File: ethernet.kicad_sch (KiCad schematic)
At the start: 37 parts, among them J200 RJ45_Hanrun_HR911105A_Horizon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, U200 LAN8742A, U201 USBLC6-4SC6, Y200 25MHz

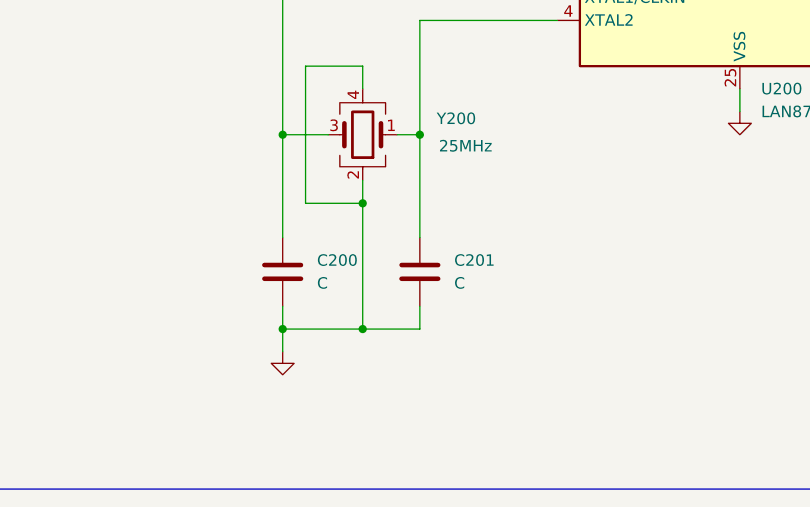
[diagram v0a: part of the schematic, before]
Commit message: Footprints added
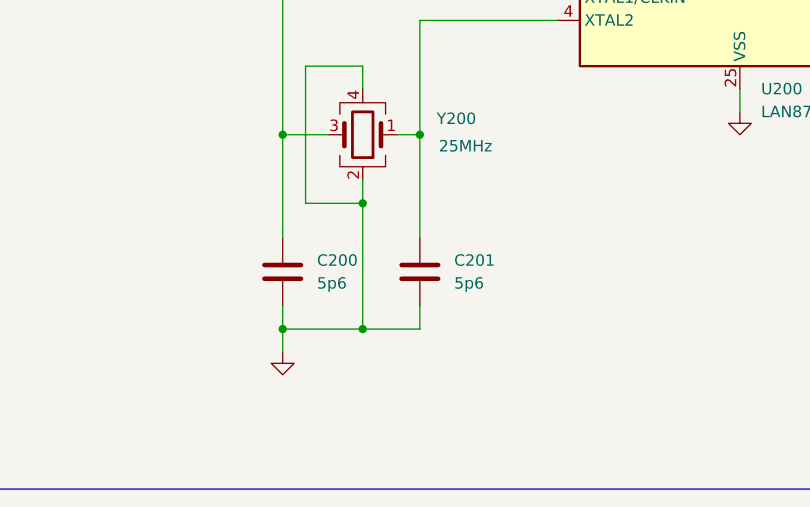
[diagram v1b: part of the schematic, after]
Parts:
- C200, C201: value C -> 5p6; footprint (none) -> Capacitor_SMD:C_01005_0402Metric
- C202: footprint (none) -> Capacitor_SMD:C_0201_0603Metric
- C203, C204, C205, C206, C207, C208, C209, C210, C211, C212: footprint (none) -> Capacitor_SMD:C_01005_0402Metric
- JP200: footprint (none) -> Jumper:SolderJumper-2_P1.3mm_Bridged_Pad1.0x1.5mm
- R200, R201, R202, R203, R204, R205, R206, R207, R208, R209, R210, R211, R212, R213, R214, R215, R216, R217, R218: footprint (none) -> Resistor_SMD:R_01005_0402Metric
- Y200: footprint (none) -> Library:CRYSTAL-SMD_4P-L2.0-W1.6-BL
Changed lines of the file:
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@@
 			)
 		)
-		(property "Footprint" ""
+		(property "Footprint" "Resistor_SMD:R_01005_0402Metric"
 			(at 40.894 85.344 90)
 			(effects
@@
 			)
 		)
-		(property "Value" "C"
+		(property "Value" "5p6"
 			(at 74.93 140.9699 0)
 			(effects
@@
 			)
 		)
-		(property "Footprint" ""
+		(property "Footprint" "Capacitor_SMD:C_01005_0402Metric"
 			(at 72.0852 143.51 0)
 			(effects
@@
 			)
 		)
-		(property "Footprint" ""
+		(property "Footprint" "Capacitor_SMD:C_0201_0603Metric"
 			(at 129.2352 50.8 0)
 			(effects
@@
 			)
 		)
-		(property "Footprint" ""
+		(property "Footprint" "Capacitor_SMD:C_01005_0402Metric"
 			(at 187.6552 97.79 0)
 			(effects
@@
 			)
 		)
-		(property "Footprint" ""
+		(property "Footprint" "Resistor_SMD:R_01005_0402Metric"
 			(at 181.356 71.374 90)
 			(effects
@@
 			)
 		)
-		(property "Footprint" ""
+		(property "Footprint" "Resistor_SMD:R_01005_0402Metric"
 			(at 40.894 103.124 90)
 			(effects
@@
 			)
 		)
-		(property "Footprint" ""
+		(property "Footprint" "Capacitor_SMD:C_01005_0402Metric"
 			(at 140.6652 50.8 0)
 			(effects
@@
 			)
 		)
-		(property "Footprint" ""
+		(property "Footprint" "Capacitor_SMD:C_01005_0402Metric"
 			(at 163.5252 50.8 0)
 			(effects
@@
 			)
 		)
-		(property "Footprint" ""
+		(property "Footprint" "Resistor_SMD:R_01005_0402Metric"
 			(at 40.894 87.884 90)
 			(effects
@@
 			)
 		)
-		(property "Footprint" ""
+		(property "Footprint" "Capacitor_SMD:C_01005_0402Metric"
 			(at 174.9552 50.8 0)
 			(effects
@@
 			)
 		)
-		(property "Footprint" ""
+		(property "Footprint" "Resistor_SMD:R_01005_0402Metric"
 			(at 40.894 82.804 90)
 			(effects
@@
 			)
 		)
-		(property "Footprint" ""
+		(property "Footprint" "Capacitor_SMD:C_01005_0402Metric"
 			(at 210.5152 97.79 0)
 			(effects
@@
 			)
 		)
-		(property "Footprint" ""
+		(property "Footprint" "Resistor_SMD:R_01005_0402Metric"
 			(at 215.646 71.374 90)
 			(effects
@@
 			)
 		)
-		(property "Footprint" ""
+		(property "Footprint" "Capacitor_SMD:C_01005_0402Metric"
 			(at 185.1152 152.4 0)
 			(effects
@@
 			)
 		)
-		(property "Footprint" ""
+		(property "Footprint" "Resistor_SMD:R_01005_0402Metric"
 			(at 163.576 100.584 90)
 			(effects
@@
 			)
 		)
-		(property "Footprint" ""
+		(property "Footprint" "Library:CRYSTAL-SMD_4P-L2.0-W1.6-BL"
 			(at 80.01 124.46 0)
 			(effects
@@
 			)
 		)
-		(property "Footprint" ""
+		(property "Footprint" "Resistor_SMD:R_01005_0402Metric"
 			(at 230.886 152.654 90)
 			(effects
@@
 			)
 		)
-		(property "Value" "C"
+		(property "Value" "5p6"
 			(at 90.17 140.9699 0)
 			(effects
@@
 			)
 		)
-		(property "Footprint" ""
+		(property "Footprint" "Capacitor_SMD:C_01005_0402Metric"
 			(at 87.3252 143.51 0)
 			(effects
@@
 			)
 		)
-		(property "Footprint" ""
+		(property "Footprint" "Resistor_SMD:R_01005_0402Metric"
 			(at 185.166 123.444 90)
 			(effects
@@
 			)
 		)
-		(property "Footprint" ""
+		(property "Footprint" "Resistor_SMD:R_01005_0402Metric"
 			(at 192.786 71.374 90)
 			(effects
@@
 			)
 		)
-		(property "Footprint" ""
+		(property "Footprint" "Capacitor_SMD:C_01005_0402Metric"
 			(at 152.0952 50.8 0)
 			(effects
@@
 			)
 		)
-		(property "Footprint" ""
+		(property "Footprint" "Resistor_SMD:R_01005_0402Metric"
 			(at 69.596 70.104 90)
 			(effects
@@
 			)
 		)
-		(property "Footprint" ""
+		(property "Footprint" "Resistor_SMD:R_01005_0402Metric"
 			(at 257.556 138.684 90)
 			(effects
@@
 			)
 		)
-		(property "Footprint" ""
+		(property "Footprint" "Capacitor_SMD:C_01005_0402Metric"
 			(at 254.9652 78.74 0)
 			(effects
@@
 			)
 		)
-		(property "Footprint" ""
+		(property "Footprint" "Capacitor_SMD:C_01005_0402Metric"
 			(at 199.0852 97.79 0)
 			(effects
@@
 			)
 		)
-		(property "Footprint" ""
+		(property "Footprint" "Capacitor_SMD:C_01005_0402Metric"
 			(at 176.2252 97.79 0)
 			(effects
@@
 			)
 		)
-		(property "Footprint" ""
+		(property "Footprint" "Resistor_SMD:R_01005_0402Metric"
 			(at 143.256 108.204 90)
 			(effects
@@
 			)
 		)
-		(property "Footprint" ""
+		(property "Footprint" "Jumper:SolderJumper-2_P1.3mm_Bridged_Pad1.0x1.5mm"
 			(at 40.64 101.6 0)
 			(effects
@@
 			)
 		)
-		(property "Footprint" ""
+		(property "Footprint" "Resistor_SMD:R_01005_0402Metric"
 			(at 78.486 70.104 90)
 			(effects
@@
 			)
 		)
-		(property "Footprint" ""
+		(property "Footprint" "Resistor_SMD:R_01005_0402Metric"
 			(at 248.666 148.844 90)
 			(effects
@@
 			)
 		)
-		(property "Footprint" ""
+		(property "Footprint" "Resistor_SMD:R_01005_0402Metric"
 			(at 51.816 70.104 90)
 			(effects
@@
 			)
 		)
-		(property "Footprint" ""
+		(property "Footprint" "Resistor_SMD:R_01005_0402Metric"
 			(at 204.216 71.374 90)
 			(effects
@@
 			)
 		)
-		(property "Footprint" ""
+		(property "Footprint" "Resistor_SMD:R_01005_0402Metric"
 			(at 60.706 70.104 90)
 			(effects
@@
 			)
 		)
-		(property "Footprint" ""
+		(property "Footprint" "Resistor_SMD:R_01005_0402Metric"
 			(at 87.376 70.104 90)
 			(effects

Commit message: Some changes to power circuitry, more layout
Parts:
- C200, C201, C203, C204, C205, C206, C207, C208, C209, C210, C211, C212: footprint Capacitor_SMD:C_01005_0402Metric -> Capacitor_SMD:C_0402_1005Metric
- C202: footprint Capacitor_SMD:C_0201_0603Metric -> Capacitor_SMD:C_0603_1608Metric
- R200, R201, R202, R203, R204, R205, R206, R207, R208, R209, R210, R211, R212, R213, R214, R215, R216, R217, R218: footprint Resistor_SMD:R_01005_0402Metric -> Resistor_SMD:R_0402_1005Metric
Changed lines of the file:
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@@
 			)
 		)
-		(property "Footprint" "Resistor_SMD:R_01005_0402Metric"
+		(property "Footprint" "Resistor_SMD:R_0402_1005Metric"
 			(at 40.894 85.344 90)
 			(effects
@@
 			)
 		)
-		(property "Footprint" "Capacitor_SMD:C_01005_0402Metric"
+		(property "Footprint" "Capacitor_SMD:C_0402_1005Metric"
 			(at 72.0852 143.51 0)
 			(effects
@@
 			)
 		)
-		(property "Footprint" "Capacitor_SMD:C_0201_0603Metric"
+		(property "Footprint" "Capacitor_SMD:C_0603_1608Metric"
 			(at 129.2352 50.8 0)
 			(effects
@@
 			)
 		)
-		(property "Footprint" "Capacitor_SMD:C_01005_0402Metric"
+		(property "Footprint" "Capacitor_SMD:C_0402_1005Metric"
 			(at 187.6552 97.79 0)
 			(effects
@@
 			)
 		)
-		(property "Footprint" "Resistor_SMD:R_01005_0402Metric"
+		(property "Footprint" "Resistor_SMD:R_0402_1005Metric"
 			(at 181.356 71.374 90)
 			(effects
@@
 			)
 		)
-		(property "Footprint" "Resistor_SMD:R_01005_0402Metric"
+		(property "Footprint" "Resistor_SMD:R_0402_1005Metric"
 			(at 40.894 103.124 90)
 			(effects
@@
 			)
 		)
-		(property "Footprint" "Capacitor_SMD:C_01005_0402Metric"
+		(property "Footprint" "Capacitor_SMD:C_0402_1005Metric"
 			(at 140.6652 50.8 0)
 			(effects
@@
 			)
 		)
-		(property "Footprint" "Capacitor_SMD:C_01005_0402Metric"
+		(property "Footprint" "Capacitor_SMD:C_0402_1005Metric"
 			(at 163.5252 50.8 0)
 			(effects
@@
 			)
 		)
-		(property "Footprint" "Resistor_SMD:R_01005_0402Metric"
+		(property "Footprint" "Resistor_SMD:R_0402_1005Metric"
 			(at 40.894 87.884 90)
 			(effects
@@
 			)
 		)
-		(property "Footprint" "Capacitor_SMD:C_01005_0402Metric"
+		(property "Footprint" "Capacitor_SMD:C_0402_1005Metric"
 			(at 174.9552 50.8 0)
 			(effects
@@
 			)
 		)
-		(property "Footprint" "Resistor_SMD:R_01005_0402Metric"
+		(property "Footprint" "Resistor_SMD:R_0402_1005Metric"
 			(at 40.894 82.804 90)
 			(effects
@@
 			)
 		)
-		(property "Footprint" "Capacitor_SMD:C_01005_0402Metric"
+		(property "Footprint" "Capacitor_SMD:C_0402_1005Metric"
 			(at 210.5152 97.79 0)
 			(effects
@@
 			)
 		)
-		(property "Footprint" "Resistor_SMD:R_01005_0402Metric"
+		(property "Footprint" "Resistor_SMD:R_0402_1005Metric"
 			(at 215.646 71.374 90)
 			(effects
@@
 			)
 		)
-		(property "Footprint" "Capacitor_SMD:C_01005_0402Metric"
+		(property "Footprint" "Capacitor_SMD:C_0402_1005Metric"
 			(at 185.1152 152.4 0)
 			(effects
@@
 			)
 		)
-		(property "Footprint" "Resistor_SMD:R_01005_0402Metric"
+		(property "Footprint" "Resistor_SMD:R_0402_1005Metric"
 			(at 163.576 100.584 90)
 			(effects
@@
 			)
 		)
-		(property "Footprint" "Resistor_SMD:R_01005_0402Metric"
+		(property "Footprint" "Resistor_SMD:R_0402_1005Metric"
 			(at 230.886 152.654 90)
 			(effects
@@
 			)
 		)
-		(property "Footprint" "Capacitor_SMD:C_01005_0402Metric"
+		(property "Footprint" "Capacitor_SMD:C_0402_1005Metric"
 			(at 87.3252 143.51 0)
 			(effects
@@
 			)
 		)
-		(property "Footprint" "Resistor_SMD:R_01005_0402Metric"
+		(property "Footprint" "Resistor_SMD:R_0402_1005Metric"
 			(at 185.166 123.444 90)
 			(effects
@@
 			)
 		)
-		(property "Footprint" "Resistor_SMD:R_01005_0402Metric"
+		(property "Footprint" "Resistor_SMD:R_0402_1005Metric"
 			(at 192.786 71.374 90)
 			(effects
@@
 			)
 		)
-		(property "Footprint" "Capacitor_SMD:C_01005_0402Metric"
+		(property "Footprint" "Capacitor_SMD:C_0402_1005Metric"
 			(at 152.0952 50.8 0)
 			(effects
@@
 			)
 		)
-		(property "Footprint" "Resistor_SMD:R_01005_0402Metric"
+		(property "Footprint" "Resistor_SMD:R_0402_1005Metric"
 			(at 69.596 70.104 90)
 			(effects
@@
 			)
 		)
-		(property "Footprint" "Resistor_SMD:R_01005_0402Metric"
+		(property "Footprint" "Resistor_SMD:R_0402_1005Metric"
 			(at 257.556 138.684 90)
 			(effects
@@
 			)
 		)
-		(property "Footprint" "Capacitor_SMD:C_01005_0402Metric"
+		(property "Footprint" "Capacitor_SMD:C_0402_1005Metric"
 			(at 254.9652 78.74 0)
 			(effects
@@
 			)
 		)
-		(property "Footprint" "Capacitor_SMD:C_01005_0402Metric"
+		(property "Footprint" "Capacitor_SMD:C_0402_1005Metric"
 			(at 199.0852 97.79 0)
 			(effects
@@
 			)
 		)
-		(property "Footprint" "Capacitor_SMD:C_01005_0402Metric"
+		(property "Footprint" "Capacitor_SMD:C_0402_1005Metric"
 			(at 176.2252 97.79 0)
 			(effects
@@
 			)
 		)
-		(property "Footprint" "Resistor_SMD:R_01005_0402Metric"
+		(property "Footprint" "Resistor_SMD:R_0402_1005Metric"
 			(at 143.256 108.204 90)
 			(effects
@@
 			)
 		)
-		(property "Footprint" "Resistor_SMD:R_01005_0402Metric"
+		(property "Footprint" "Resistor_SMD:R_0402_1005Metric"
 			(at 78.486 70.104 90)
 			(effects
@@
 			)
 		)
-		(property "Footprint" "Resistor_SMD:R_01005_0402Metric"
+		(property "Footprint" "Resistor_SMD:R_0402_1005Metric"
 			(at 248.666 148.844 90)
 			(effects
@@
 			)
 		)
-		(property "Footprint" "Resistor_SMD:R_01005_0402Metric"
+		(property "Footprint" "Resistor_SMD:R_0402_1005Metric"
 			(at 51.816 70.104 90)
 			(effects
@@
 			)
 		)
-		(property "Footprint" "Resistor_SMD:R_01005_0402Metric"
+		(property "Footprint" "Resistor_SMD:R_0402_1005Metric"
 			(at 204.216 71.374 90)
 			(effects
@@
 			)
 		)
-		(property "Footprint" "Resistor_SMD:R_01005_0402Metric"
+		(property "Footprint" "Resistor_SMD:R_0402_1005Metric"
 			(at 60.706 70.104 90)
 			(effects
@@
 			)
 		)
-		(property "Footprint" "Resistor_SMD:R_01005_0402Metric"
+		(property "Footprint" "Resistor_SMD:R_0402_1005Metric"
 			(at 87.376 70.104 90)
 			(effects

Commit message: Extremely incomplete, preliminary, pre-alpha, ugly layout
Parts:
- removed C207, C209, C210, C211: 10p, Capacitor_SMD:C_0402_1005Metric, symbol Device:C
- renumbered C208 to C207, C212 to C208
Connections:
- net TX+: now also U201.3 (I/O2); no longer U201.1 (I/O1)
- net TX-: now also U201.1 (I/O1); no longer U201.3 (I/O2)
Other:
- moved on the sheet: C208, U201

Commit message: First decent layout
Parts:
- J200: footprint Connector_RJ:RJ45_Hanrun_HR911105A_Horizontal -> Library:RJ45_Hanrun_HR911105A_Horizontal
- U200: footprint Package_DFN_QFN:VQFN-24-1EP_4x4mm_P0.5mm_EP2.5x2.5mm_ThermalVias -> Library:VQFN-24-1EP_4x4mm_P0.5mm_EP2.5x2.5mm_ThermalVias
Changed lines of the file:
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@@
 			)
 		)
-		(property "Footprint" "Connector_RJ:RJ45_Hanrun_HR911105A_Horizontal"
+		(property "Footprint" "Library:RJ45_Hanrun_HR911105A_Horizontal"
 			(at 214.63 124.46 0)
 			(effects
@@
 			)
 		)
-		(property "Footprint" "Package_DFN_QFN:VQFN-24-1EP_4x4mm_P0.5mm_EP2.5x2.5mm_ThermalVias"
+		(property "Footprint" "Library:VQFN-24-1EP_4x4mm_P0.5mm_EP2.5x2.5mm_ThermalVias"
 			(at 123.19 118.11 0)
 			(effects

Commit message: First workable layout
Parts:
- C200, C201: value 5p6 -> 10p; LCSC (none) -> C32949
- C202: LCSC (none) -> C19702
- C203, C204, C205, C206, C208: LCSC (none) -> C1525
- C207: LCSC (none) -> C337699
- J200: LCSC (none) -> C12074
- R200, R201, R203: LCSC (none) -> C138002
- R202, R204, R205, R206, R207, R208, R209: LCSC (none) -> C60490
- R210: LCSC (none) -> C25852
- R211, R213, R214, R215: LCSC (none) -> C87044
- R212, R216: LCSC (none) -> C106231
- R217, R218: LCSC (none) -> C105875
- U200: LCSC (none) -> C220794
- U201: LCSC (none) -> C111212
- Y200: LCSC (none) -> C5765970

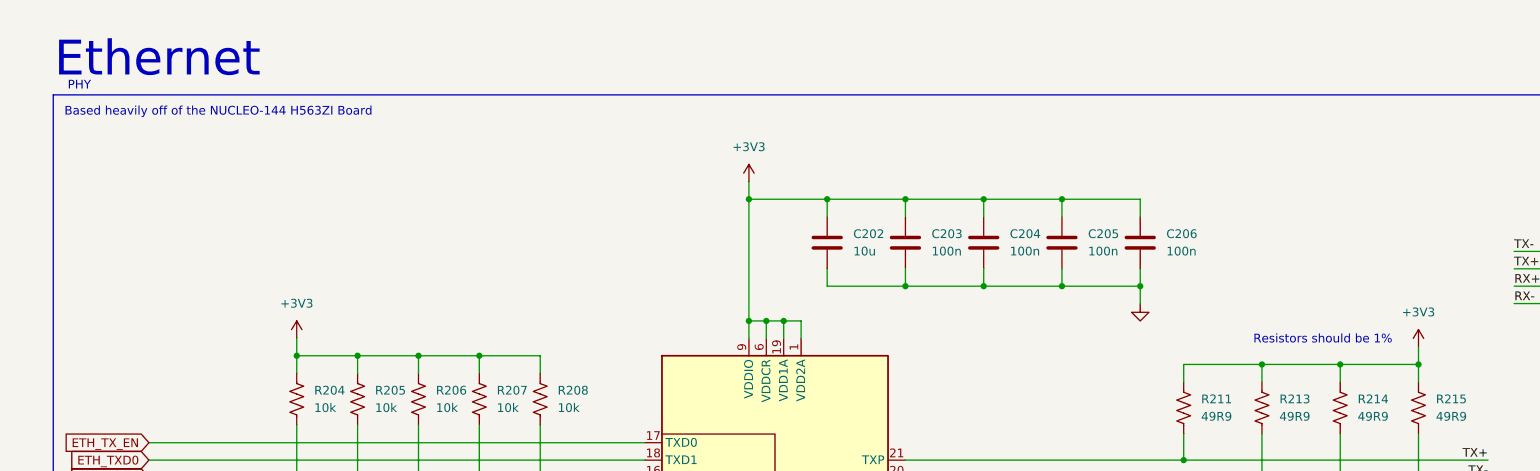
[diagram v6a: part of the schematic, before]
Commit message: Modify repo for usage on Linux, add basic CI
chore: fix CI

Small things
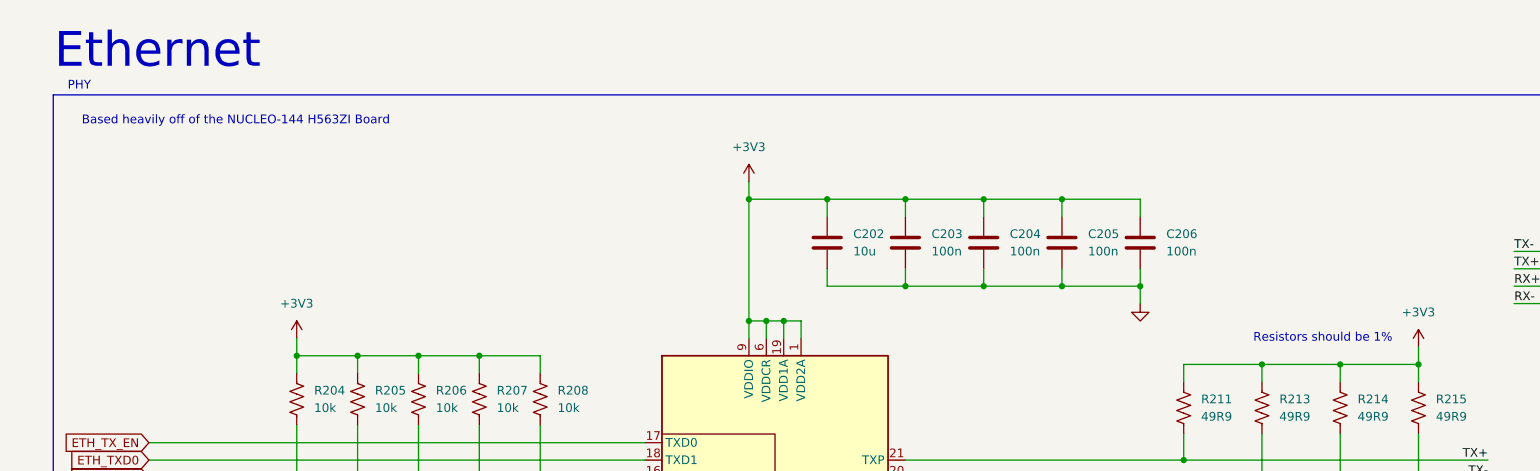
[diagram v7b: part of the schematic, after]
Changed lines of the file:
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@@
 	(text "Based heavily off of the NUCLEO-144 H563ZI Board"
 		(exclude_from_sim no)
-		(at 39.37 27.94 0)
+		(at 41.91 29.21 0)
 		(effects
 			(font
@@
 	(text "Ethernet"
 		(exclude_from_sim no)
-		(at 30.48 20.32 0)
+		(at 30.48 19.05 0)
 		(effects
 			(font
@@
 	(text "Resistors should be 1%"
 		(exclude_from_sim no)
-		(at 200.66 61.214 0)
+		(at 200.66 60.96 0)
 		(effects
 			(font
